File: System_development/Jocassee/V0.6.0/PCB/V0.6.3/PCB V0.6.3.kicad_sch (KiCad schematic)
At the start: 30 parts, among them J1 TDS PRB, J2 Temp, J3 BAT, J4 TRBDT, J5 CHRG, J6 Conn_Coaxial_Small, P1 SD card socket, Q1 2N2222A, U1 NRF24L01+PA+LNA, U2 ProMicro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

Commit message: Code folders created
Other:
- note added: "10"
- note added: "14"
- note added: "15"
- note added: "16"
- note added: "2"
- note added: "3"
- note added: "4"
- note added: "5"
- note added: "6"
- note added: "7"
- note added: "8"
- note added: "9"
- note added: "A0"
- note added: "A1"
- note added: "A2"
- note added: "A3"
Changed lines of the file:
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@@
+		)
+	)
+	(text "6"
+		(exclude_from_sim no)
+		(at 87.376 151.384 0)
+		(effects
+			(font
+				(size 1.27 1.27)
+			)
+		)
+	)
+	(text "A1"
+		(exclude_from_sim no)
+		(at 101.6 146.304 0)
+		(effects
+			(font
+				(size 1.27 1.27)
+			)
+		)
+	)
+	(text "A2"
+		(exclude_from_sim no)
+		(at 101.6 143.764 0)
+		(effects
+			(font
+				(size 1.27 1.27)
+			)
+		)
+	)
+	(text "14"
+		(exclude_from_sim no)
+		(at 101.6 153.924 0)
+		(effects
+			(font
+				(size 1.27 1.27)
+			)
+		)
+	)
+	(text "4"
+		(exclude_from_sim no)
+		(at 87.376 146.304 0)
+		(effects
+			(font
+				(size 1.27 1.27)
+			)
+		)
+	)
+	(text "3"
+		(exclude_from_sim no)
+		(at 87.376 143.764 0)
+		(effects
+			(font
+				(size 1.27 1.27)
+			)
+		)
+	)
+	(text "9"
+		(exclude_from_sim no)
+		(at 87.376 159.004 0)
+		(effects
+			(font
+				(size 1.27 1.27)
+			)
+		)
+	)
+	(text "A0"
+		(exclude_from_sim no)
+		(at 101.6 148.844 0)
+		(effects
+			(font
+				(size 1.27 1.27)
+			)
+		)
+	)
+	(text "7"
+		(exclude_from_sim no)
+		(at 87.376 153.924 0)
+		(effects
+			(font
+				(size 1.27 1.27)
+			)
+		)
+	)
+	(text "8"
+		(exclude_from_sim no)
+		(at 87.376 156.464 0)
+		(effects
+			(font
+				(size 1.27 1.27)
+			)
+		)
+	)
+	(text "2"
+		(exclude_from_sim no)
+		(at 87.376 141.224 0)
+		(effects
+			(font
+				(size 1.27 1.27)
+			)
+		)
+	)
+	(text "5"
+		(exclude_from_sim no)
+		(at 87.376 148.844 0)
+		(effects
+			(font
+				(size 1.27 1.27)
+			)
+		)
+	)
+	(text "15"
+		(exclude_from_sim no)
+		(at 101.6 151.384 0)
+		(effects
+			(font
+				(size 1.27 1.27)
+			)
+		)
+	)
+	(text "10"
+		(exclude_from_sim no)
+		(at 101.6 159.004 0)
+		(effects
+			(font
+				(size 1.27 1.27)
+			)
+		)
+	)
+	(text "16"
+		(exclude_from_sim no)
+		(at 101.6 156.464 0)
+		(effects
+			(font
+				(size 1.27 1.27)
+			)
+		)
+	)
+	(text "A3"
+		(exclude_from_sim no)
+		(at 101.6 141.224 0)
+		(effects
+			(font
+				(size 1.27 1.27)
+			)
 		)
 	)

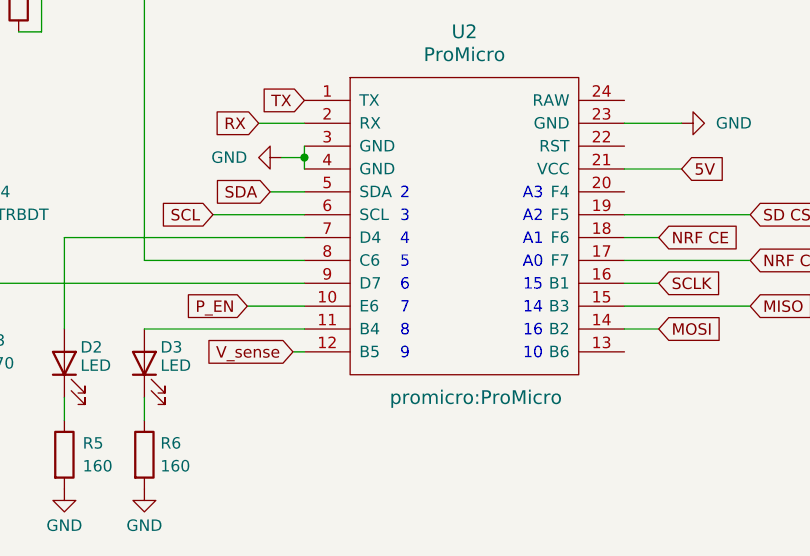
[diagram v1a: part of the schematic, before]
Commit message: MCU pin notation corrected.
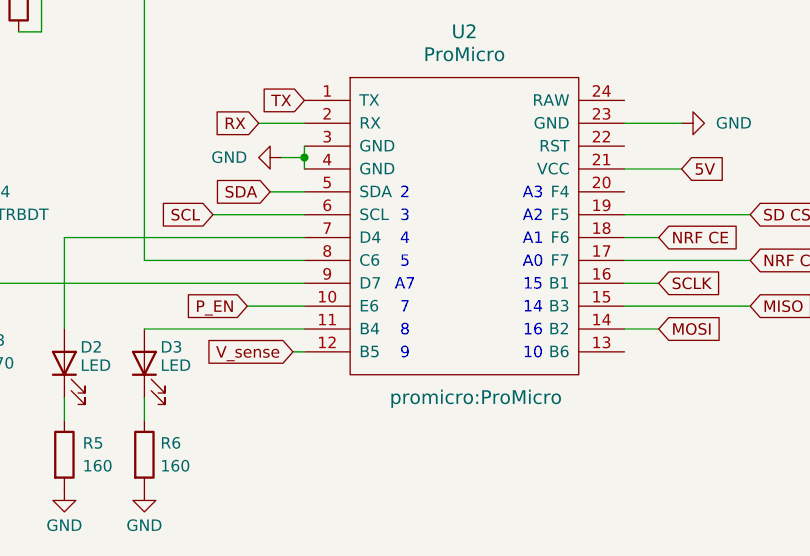
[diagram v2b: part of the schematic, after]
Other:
- note added: "A7"
- note removed: "6"
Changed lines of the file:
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@@
 		)
 	)
-	(text "6"
+	(text "A7"
 		(exclude_from_sim no)
 		(at 87.376 151.384 0)
